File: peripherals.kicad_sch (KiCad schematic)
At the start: 6 parts, among them J1 WE_68715014522

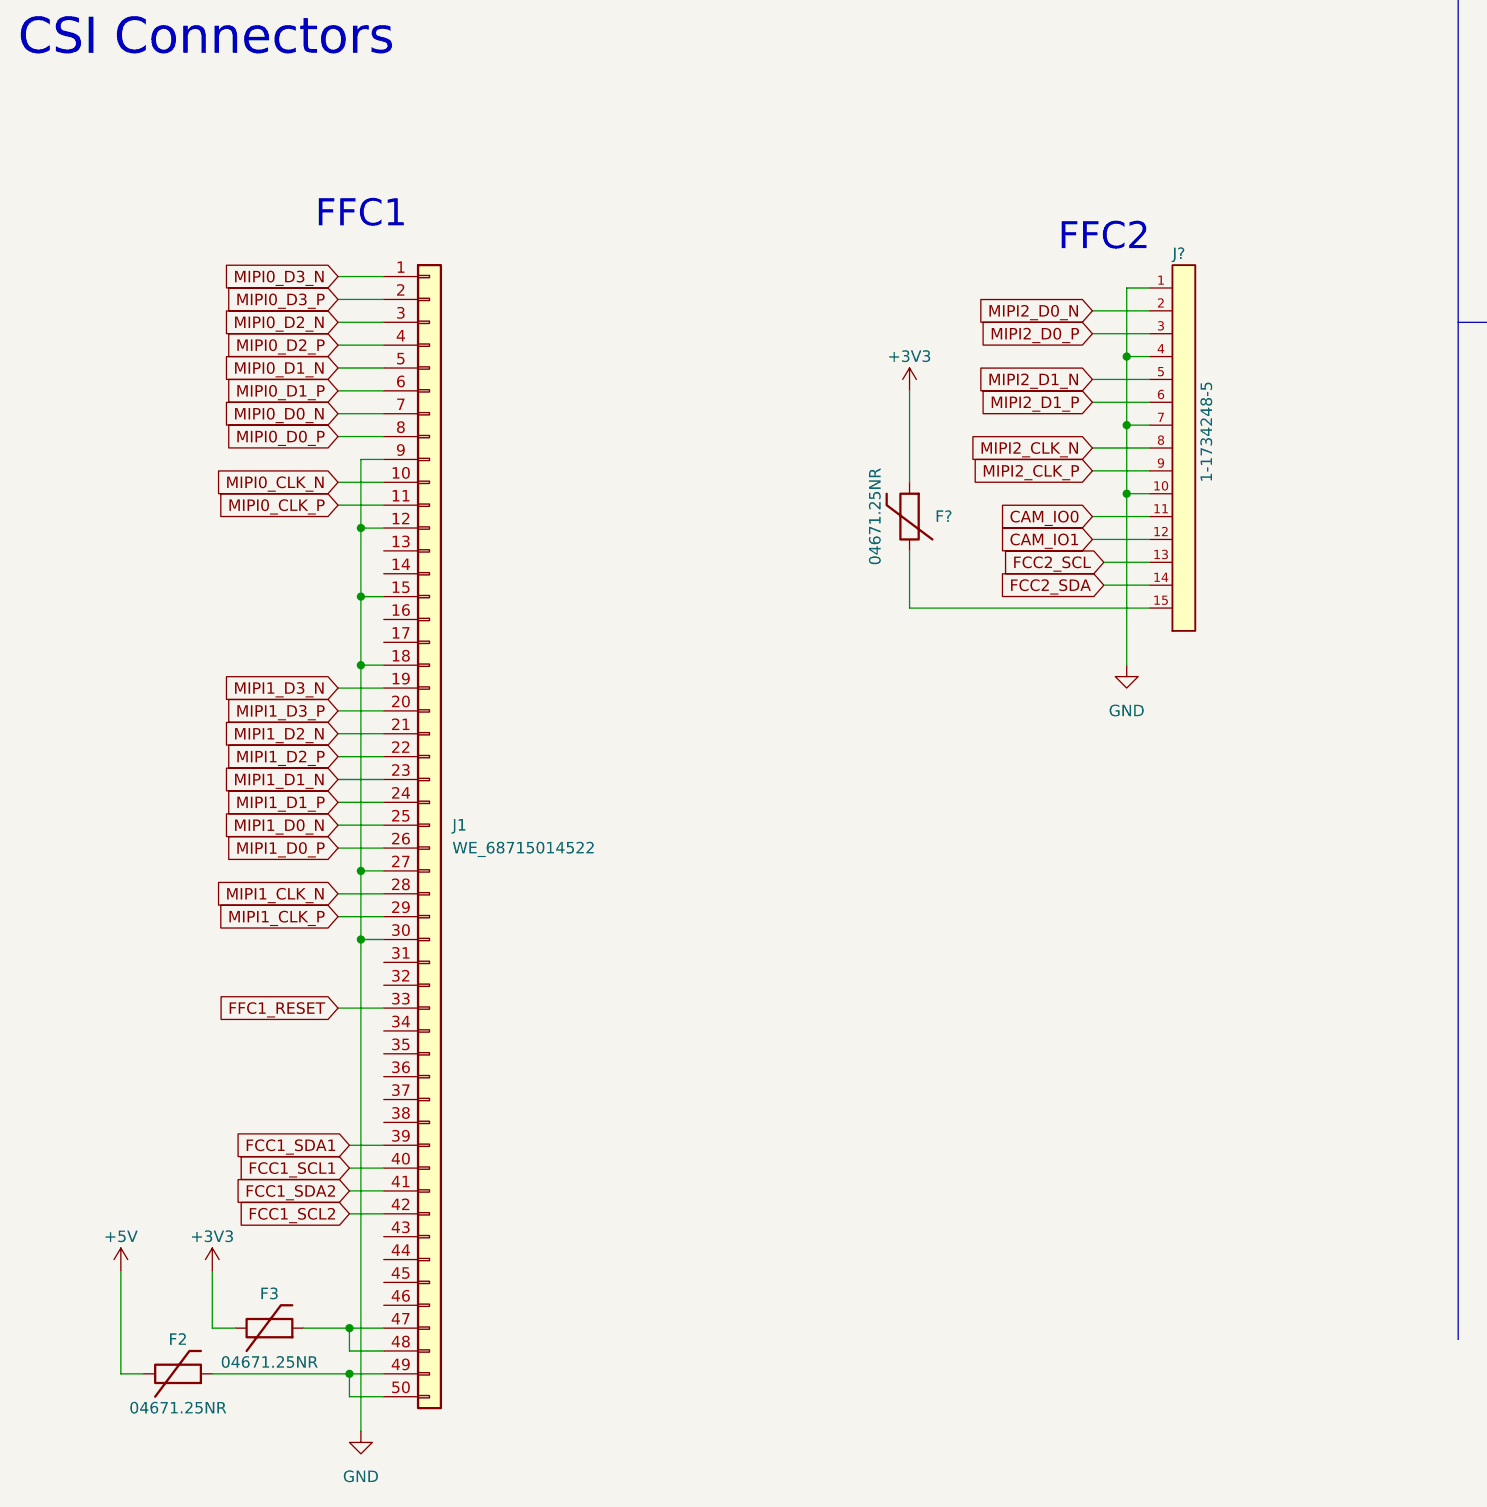
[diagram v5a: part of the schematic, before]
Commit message: Replaced RPi camera connector with 50pin one, modified PSU with ability of being supplied via FFC
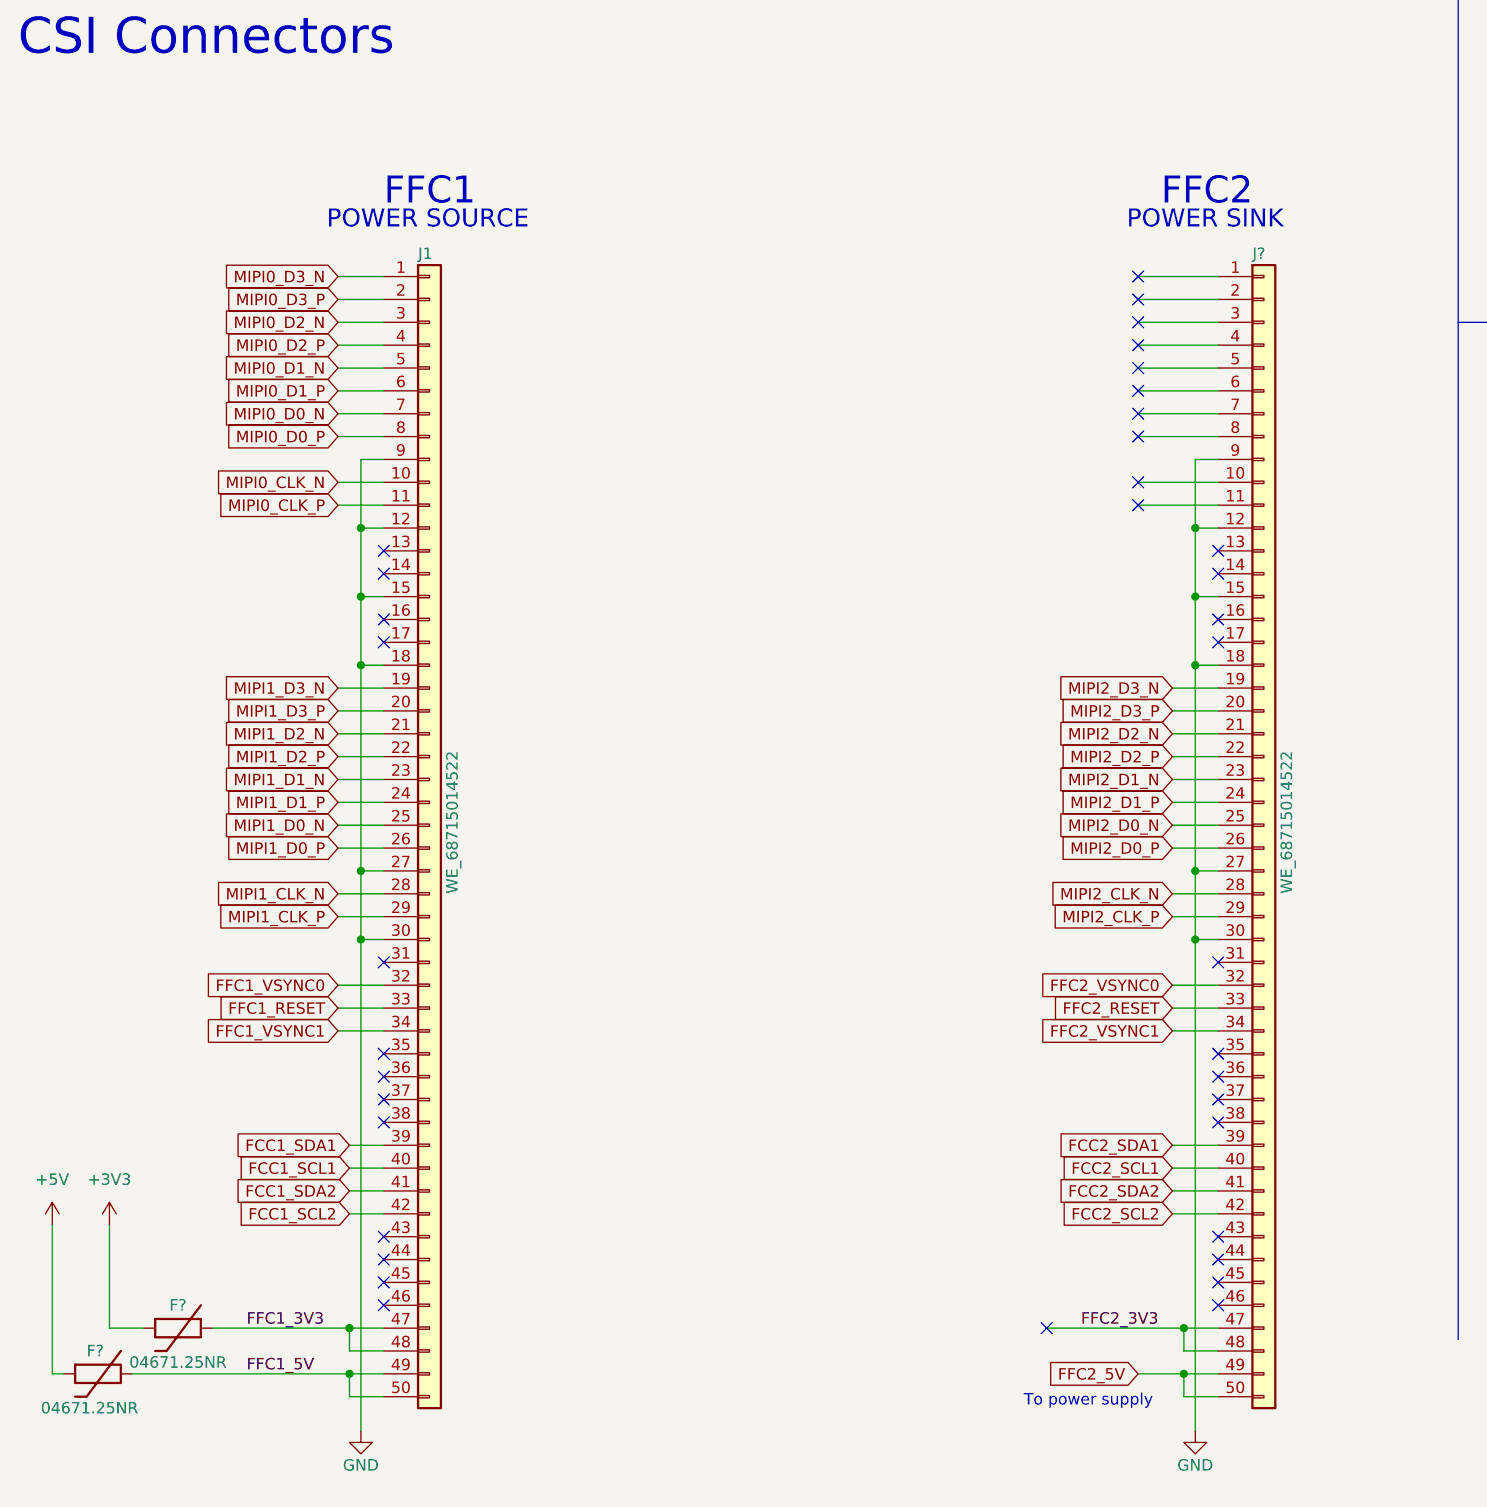
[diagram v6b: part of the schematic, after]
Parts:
- removed F2, F3, F?: 04671.25NR, antmicro-footprints:0603-Fuse-Littelfuse-0467, symbol antmicroFuses:04671.25NR
- removed J?: 1-1734248-5, antmicro-footprints:TE_1-1734248-5, symbol antmicroFCCConnectors:1-1734248-5
- added F? (x2): 04671.25NR, antmicro-footprints:0603-Fuse-Littelfuse-0467, symbol antmicroFuses:04671.25NR
- added J?: WE_68715014522, antmicro-footprints:WE_68715014522, symbol antmicroFCCConnectors:WE_68715014522
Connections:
- net +3V3: now also F?.2
- net +5V: now also F?.2
- net GND: now also J?.12 (Pin_12), J?.15 (Pin_15), J?.18 (Pin_18), J?.27 (Pin_27), J?.30 (Pin_30), J?.9 (Pin_9)
- net MIPI2_CLK_N: now also J?.28 (Pin_28)
- net MIPI2_CLK_P: now also J?.29 (Pin_29)
- net MIPI2_D0_N: now also J?.25 (Pin_25)
- net MIPI2_D0_P: now also J?.26 (Pin_26)
- net MIPI2_D1_N: now also J?.23 (Pin_23)
- net MIPI2_D1_P: now also J?.24 (Pin_24)
- net FFC1_3V3: now reaches J1.47 (Pin_47), J1.48 (Pin_48)
- net FFC1_3V3: now also F?.1
- net FFC1_5V: now reaches J1.49 (Pin_49), J1.50 (Pin_50)
- net FFC1_5V: now also F?.1
- net FFC1_VSYNC0: now reaches J1.32 (Pin_32)
- net FFC1_VSYNC1: now reaches J1.34 (Pin_34)
- new net FCC2_SCL1: J?.40 (Pin_40)
- new net FCC2_SCL2: J?.42 (Pin_42)
- new net FCC2_SDA1: J?.39 (Pin_39)
- new net FCC2_SDA2: J?.41 (Pin_41)
- new net FFC2_3V3: J?.47 (Pin_47), J?.48 (Pin_48)
- new net FFC2_5V: J?.49 (Pin_49), J?.50 (Pin_50)
- new net FFC2_RESET: J?.33 (Pin_33)
- new net FFC2_VSYNC0: J?.32 (Pin_32)
- new net FFC2_VSYNC1: J?.34 (Pin_34)
- new net MIPI2_D2_N: J?.21 (Pin_21)
- new net MIPI2_D2_P: J?.22 (Pin_22)
- new net MIPI2_D3_N: J?.19 (Pin_19)
- new net MIPI2_D3_P: J?.20 (Pin_20)
- no-connect marks 0 -> 37
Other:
- note added: "POWER SINK"
- note added: "POWER SOURCE"
- note added: "To power supply"

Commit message: Added indicator LEDs and user switch
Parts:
- added D? (x2): LTST-C190GKT, antmicro-footprints:LED_0603, symbol antmicroLEDIndicationDiscrete:LTST-C190GKT
- added R? (x2): R_470R_0603, antmicro-footprints:0603-res, symbol antmicroResistors0603:R_470R_0603
- added SW?: SW_DIP_x06, antmicro-footprints:SW_SPST_6_Slide_MCDHN-06F-T-V_P1.27mm, symbol antmicroSlideSwitches:SW_DIP_x06
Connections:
- net GND: now also D?.2, D?.2, SW?.10, SW?.11, SW?.12, SW?.7, SW?.8, SW?.9
- new net: D?.1, R?.1 (x2)
- new net DIP0: SW?.1
- new net DIP1: SW?.2
- new net DIP2: SW?.3
- new net DIP3: SW?.4
- new net DIP4: SW?.5
- new net DIP5: SW?.6
- new net LED0: R?.2
- new net LED1: R?.2
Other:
- note added: "USER LEDs"
- note added: "USER SWITCH"
- moved on the sheet: F?, J1, J?
